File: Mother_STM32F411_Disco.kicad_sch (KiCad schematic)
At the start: 34 parts, among them U1 ESP32-DEVKIT-V1

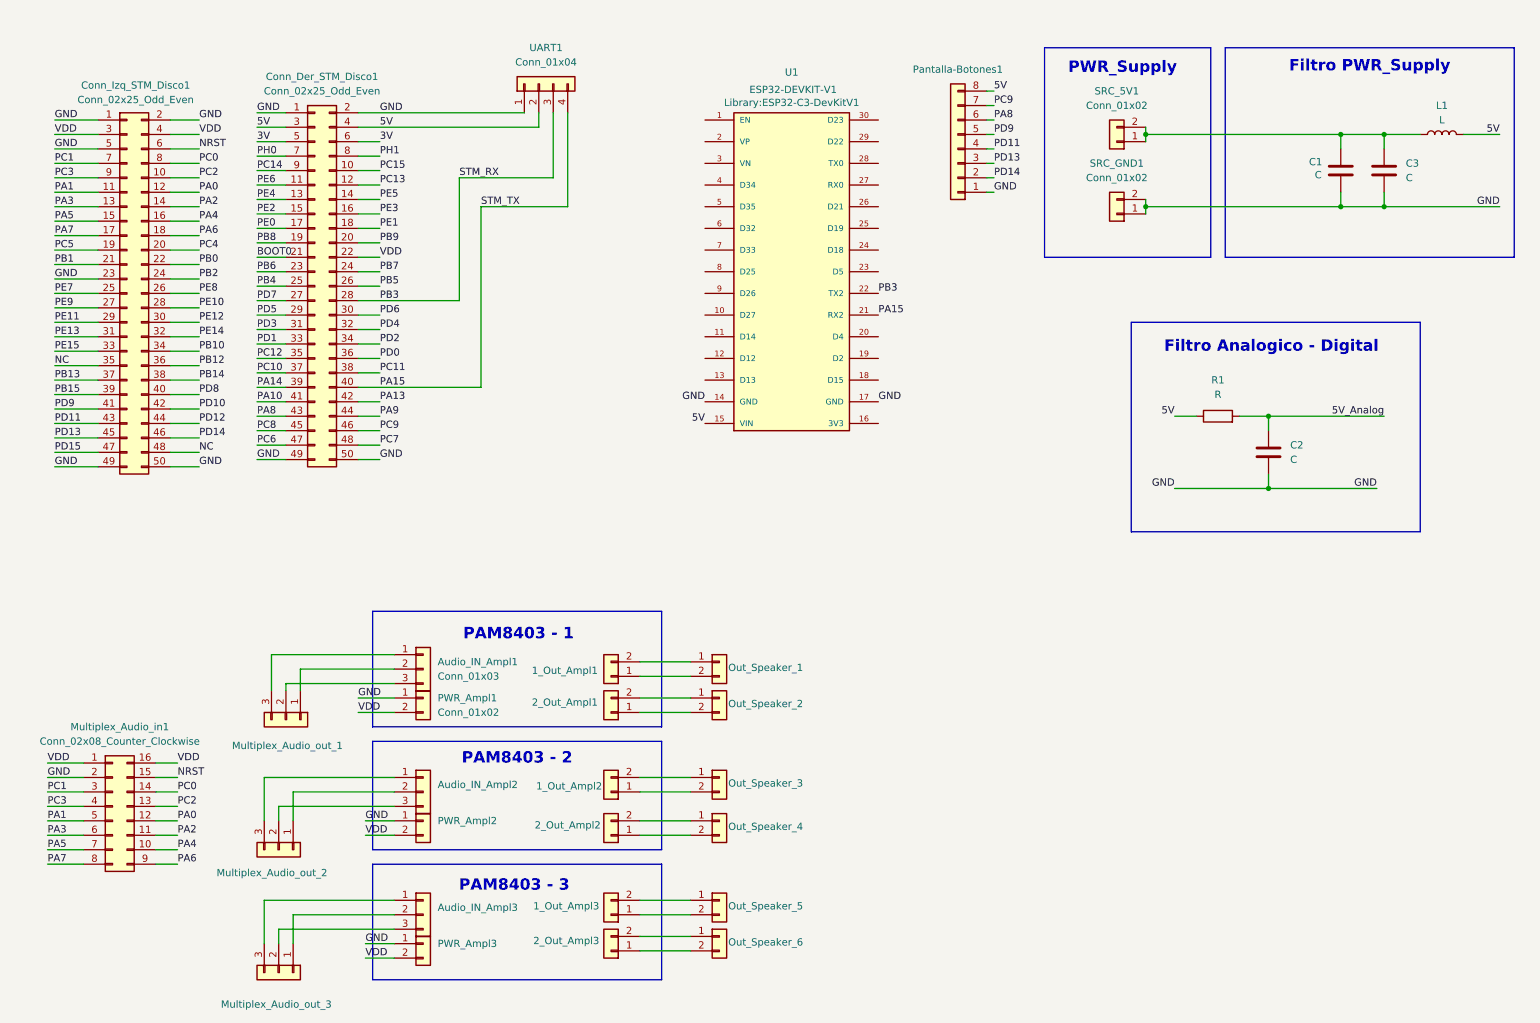
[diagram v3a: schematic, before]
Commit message: Placa lista para ser routeada con pistas
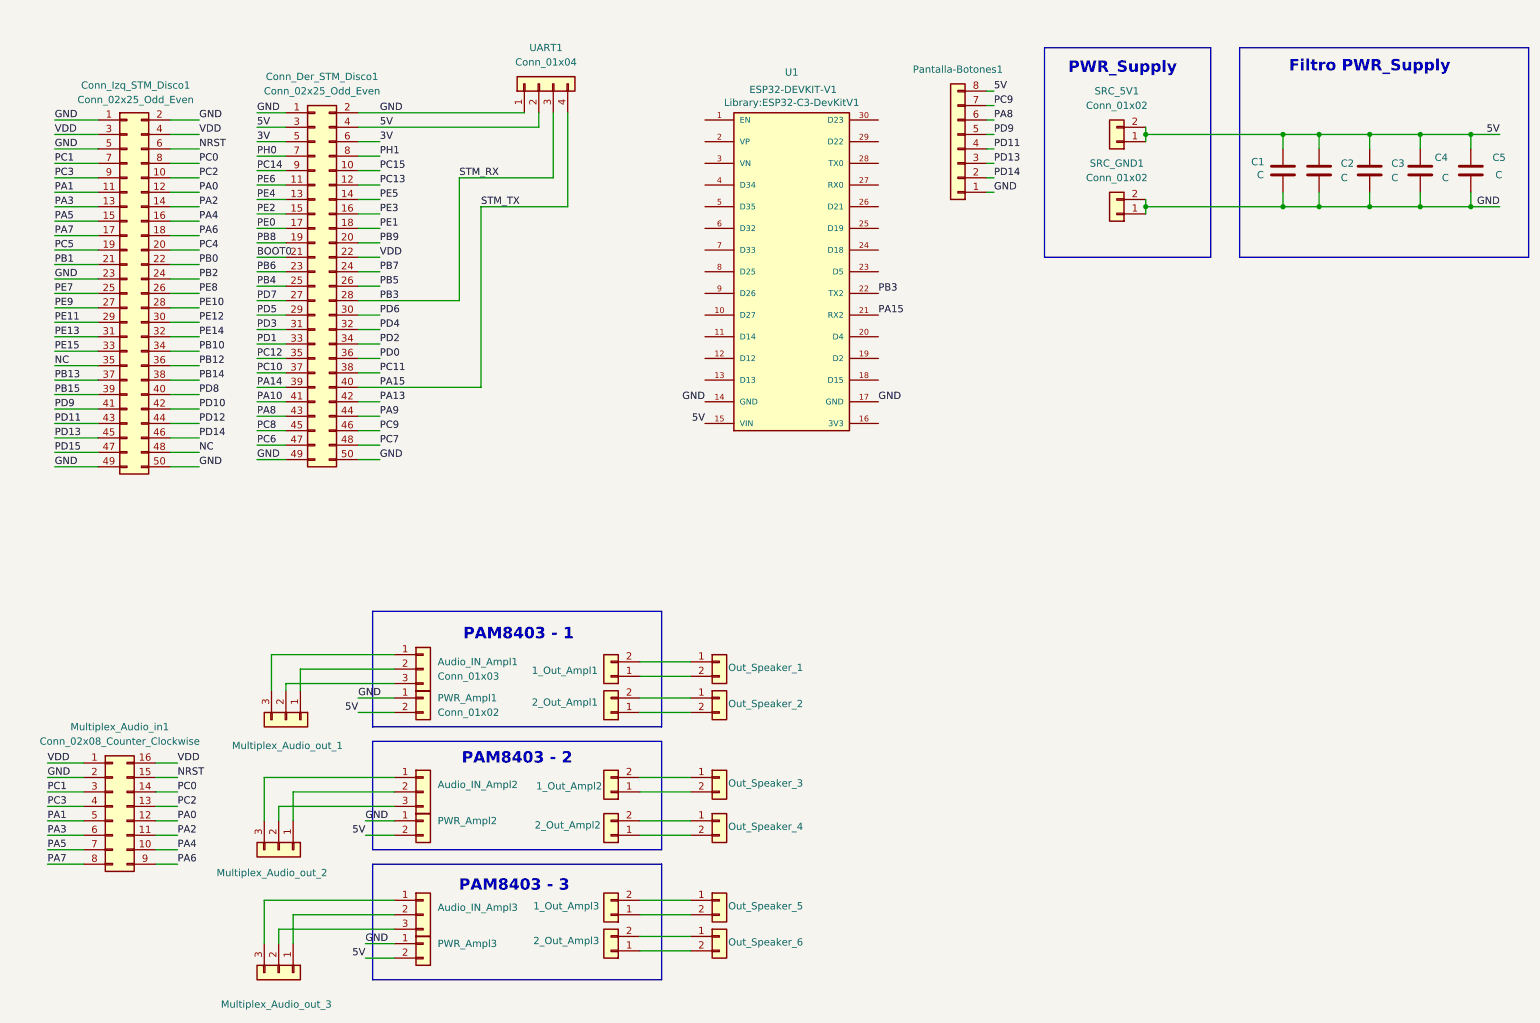
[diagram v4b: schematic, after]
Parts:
- removed L1: L, Inductor_THT:Choke_Schaffner_RN102-04-14.0x14.0mm, symbol Device:L
- removed R1: R, Resistor_SMD:R_0805_2012Metric_Pad1.20x1.40mm_HandSolder, symbol Device:R
- added C4: C, Capacitor_THT:C_Disc_D8.0mm_W5.0mm_P5.00mm, symbol Device:C
- added C5: C, Capacitor_THT:CP_Radial_D13.0mm_P5.00mm, symbol Device:C
- C2: footprint Capacitor_SMD:C_0805_2012Metric_Pad1.18x1.45mm_HandSolder -> Capacitor_THT:C_Disc_D8.0mm_W5.0mm_P5.00mm
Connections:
- net 5V_Analog is gone; now on net 5V: C2.1
- net 5V: now also C1.1, C3.1, PWR_Ampl1.2 (Pin_2), PWR_Ampl2.2 (Pin_2), PWR_Ampl3.2 (Pin_2), SRC_5V1.1 (Pin_1), SRC_5V1.2 (Pin_2), C4.1, C5.1
- net GND: now also C4.2, C5.2
- net VDD: no longer PWR_Ampl1.2 (Pin_2), PWR_Ampl2.2 (Pin_2), PWR_Ampl3.2 (Pin_2)
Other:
- note removed: "Filtro Analogico - Digital"
- moved on the sheet: C1, C3

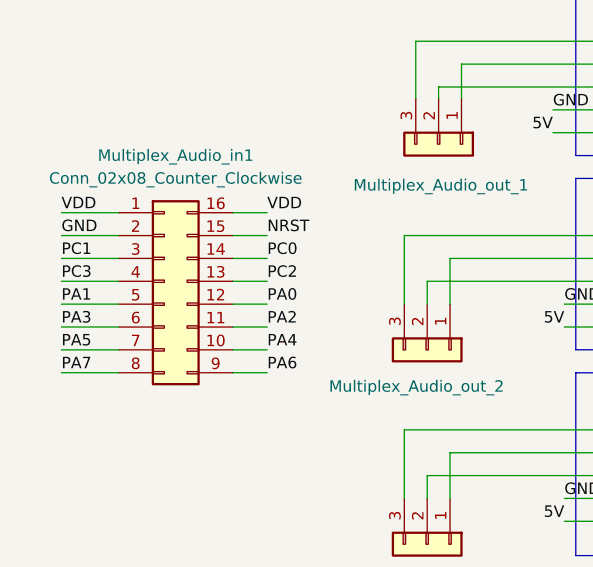
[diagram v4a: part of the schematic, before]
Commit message: acomodando  pines de la placa stm
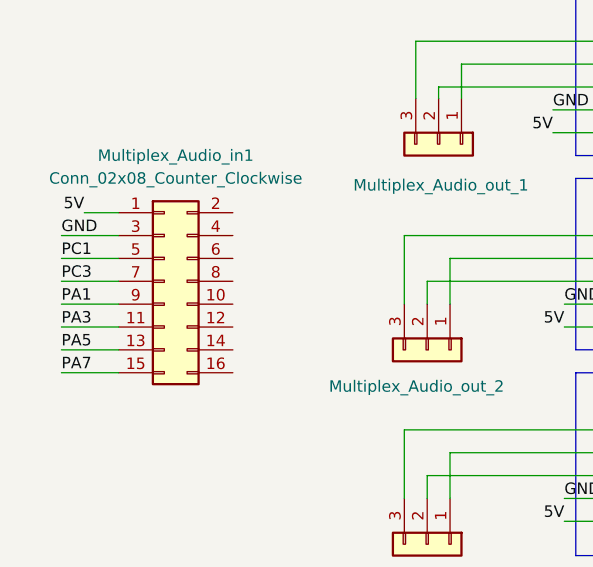
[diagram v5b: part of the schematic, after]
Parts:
- Multiplex_Audio_in1: symbol Connector_Generic:Conn_02x08_Counter_Clockwise -> Connector_Generic:Conn_02x08_Odd_Even
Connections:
- net 5V: now also Multiplex_Audio_in1.1 (Pin_1)
- net GND: now also Multiplex_Audio_in1.3 (Pin_3); no longer Multiplex_Audio_in1.2 (Pin_2)
- net NRST: no longer Multiplex_Audio_in1.15 (Pin_15)
- net PA0: no longer Multiplex_Audio_in1.12 (Pin_12)
- net PA1: now also Multiplex_Audio_in1.9 (Pin_9); no longer Multiplex_Audio_in1.5 (Pin_5)
- net PA2: no longer Multiplex_Audio_in1.11 (Pin_11)
- net PA3: now also Multiplex_Audio_in1.11 (Pin_11); no longer Multiplex_Audio_in1.6 (Pin_6)
- net PA4: no longer Multiplex_Audio_in1.10 (Pin_10)
- net PA5: now also Multiplex_Audio_in1.13 (Pin_13); no longer Multiplex_Audio_in1.7 (Pin_7)
- net PA6: no longer Multiplex_Audio_in1.9 (Pin_9)
- net PA7: now also Multiplex_Audio_in1.15 (Pin_15); no longer Multiplex_Audio_in1.8 (Pin_8)
- net PC0: no longer Multiplex_Audio_in1.14 (Pin_14)
- net PC1: now also Multiplex_Audio_in1.5 (Pin_5); no longer Multiplex_Audio_in1.3 (Pin_3)
- net PC2: no longer Multiplex_Audio_in1.13 (Pin_13)
- net PC3: now also Multiplex_Audio_in1.7 (Pin_7); no longer Multiplex_Audio_in1.4 (Pin_4)
- net VDD: no longer Multiplex_Audio_in1.1 (Pin_1), Multiplex_Audio_in1.16 (Pin_16)
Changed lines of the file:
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@@
 	(wire
 		(pts
-			(xy 40.64 168.91) (xy 44.45 168.91)
-		)
-		(stroke
-			(width 0)
-			(type default)
-		)
-	)
-	(wire
-		(pts
 			(xy 214.63 41.91) (xy 214.63 43.18)
 		)
@@
 	(wire
 		(pts
-			(xy 40.64 161.29) (xy 44.45 161.29)
-		)
-		(stroke
-			(width 0)
-			(type default)
-		)
-	)
-	(wire
-		(pts
 			(xy 214.63 43.18) (xy 238.76 43.18)
 		)
@@
 	(wire
 		(pts
-			(xy 40.64 171.45) (xy 44.45 171.45)
-		)
-		(stroke
-			(width 0)
-			(type default)
-		)
-	)
-	(wire
-		(pts
 			(xy 58.42 69.85) (xy 63.5 69.85)
 		)
@@
 	(wire
 		(pts
-			(xy 40.64 163.83) (xy 44.45 163.83)
-		)
-		(stroke
-			(width 0)
-			(type default)
-		)
-	)
-	(wire
-		(pts
 			(xy 76.2 72.39) (xy 93.98 72.39)
 		)
@@
 	(wire
 		(pts
-			(xy 40.64 158.75) (xy 44.45 158.75)
-		)
-		(stroke
-			(width 0)
-			(type default)
-		)
-	)
-	(wire
-		(pts
 			(xy 22.86 58.42) (xy 30.48 58.42)
 		)
@@
 	(wire
 		(pts
-			(xy 40.64 166.37) (xy 44.45 166.37)
-		)
-		(stroke
-			(width 0)
-			(type default)
-		)
-	)
-	(wire
-		(pts
 			(xy 238.76 43.18) (xy 245.11 43.18)
 		)
@@
 	(wire
 		(pts
-			(xy 40.64 156.21) (xy 44.45 156.21)
-		)
-		(stroke
-			(width 0)
-			(type default)
-		)
-	)
-	(wire
-		(pts
 			(xy 22.86 48.26) (xy 30.48 48.26)
 		)
@@
 	(wire
 		(pts
-			(xy 40.64 153.67) (xy 44.45 153.67)
-		)
-		(stroke
-			(width 0)
-			(type default)
-		)
-	)
-	(wire
-		(pts
 			(xy 43.18 58.42) (xy 48.26 58.42)
 		)
@@
 	(wire
 		(pts
-			(xy 21.59 153.67) (xy 27.94 153.67)
+			(xy 24.13 153.67) (xy 27.94 153.67)
 		)
 		(stroke
@@
 		)
 	)
-	(label "PA0"
-		(at 44.45 163.83 0)
-		(effects
-			(font
-				(size 1.27 1.27)
-			)
-			(justify left bottom)
-		)
-	)
 	(label "STM_RX"
 		(at 93.98 50.8 0)
@@
 		)
 	)
-	(label "VDD"
-		(at 44.45 153.67 0)
-		(effects
-			(font
-				(size 1.27 1.27)
-			)
-			(justify left bottom)
-		)
-	)
 	(label "PE15"
 		(at 22.86 81.28 0)
@@
 		)
 	)
+	(label "5V"
+		(at 24.13 153.67 180)
+		(effects
+			(font
+				(size 1.27 1.27)
+			)
+			(justify right bottom)
+		)
+	)
 	(label "PA5"
 		(at 21.59 168.91 0)
@@
 		)
 	)
-	(label "VDD"
-		(at 21.59 153.67 0)
-		(effects
-			(font
-				(size 1.27 1.27)
-			)
-			(justify left bottom)
-		)
-	)
 	(label "PD11"
 		(at 187.96 45.72 0)
@@
 		)
 	)
-	(label "PA4"
-		(at 44.45 168.91 0)
-		(effects
-			(font
-				(size 1.27 1.27)
-			)
-			(justify left bottom)
-		)
-	)
 	(label "PA8"
 		(at 58.42 92.71 0)
@@
 		)
 	)
-	(label "PA2"
-		(at 44.45 166.37 0)
-		(effects
-			(font
-				(size 1.27 1.27)
-			)
-			(justify left bottom)
-		)
-	)
 	(label "PB14"
 		(at 48.26 86.36 0)
@@
 		)
 	)
-	(label "NRST"
-		(at 44.45 156.21 0)
-		(effects
-			(font
-				(size 1.27 1.27)
-			)
-			(justify left bottom)
-		)
-	)
 	(label "PA7"
 		(at 21.59 171.45 0)
@@
 		)
 	)
-	(label "PA6"
-		(at 44.45 171.45 0)
-		(effects
-			(font
-				(size 1.27 1.27)
-			)
-			(justify left bottom)
-		)
-	)
 	(label "PD8"
 		(at 48.26 88.9 0)
@@
 		)
 	)
-	(label "PC0"
-		(at 44.45 158.75 0)
-		(effects
-			(font
-				(size 1.27 1.27)
-			)
-			(justify left bottom)
-		)
-	)
 	(label "PH1"
 		(at 80.01 46.99 0)
@@
 		)
 	)
-	(label "PC2"
-		(at 44.45 161.29 0)
-		(effects
-			(font
-				(size 1.27 1.27)
-			)
-			(justify left bottom)
-		)
-	)
 	(label "GND"
 		(at 58.42 39.37 0)
@@
 	)
 	(symbol
-		(lib_id "Connector_Generic:Conn_02x08_Counter_Clockwise")
+		(lib_id "Connector_Generic:Conn_02x08_Odd_Even")
 		(at 33.02 161.29 0)
 		(unit 1)
@@
 			)
 		)
-		(property "Description" "Generic connector, double row, 02x08, counter clockwise pin numbering scheme (similar to DIP package numbering), script generated (kicad-library-utils/schlib/autogen/connector/)"
+		(property "Description" "Generic connector, double row, 02x08, odd/even pin numbering scheme (row 1 odd numbers, row 2 even numbers), script generated (kicad-library-utils/schlib/autogen/connector/)"
 			(at 33.02 161.29 0)
 			(effects
